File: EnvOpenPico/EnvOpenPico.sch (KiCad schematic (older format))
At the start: 54 parts, among them J2 SKRKAEE020, J3 2.54mm header 01x20, J4 2.54mm header 01x20, J5 Conn_01x03_Male, Q1 Si2329DS, U1 TLV75533PDBVR, U3 RP2040, Y1 3225_4P

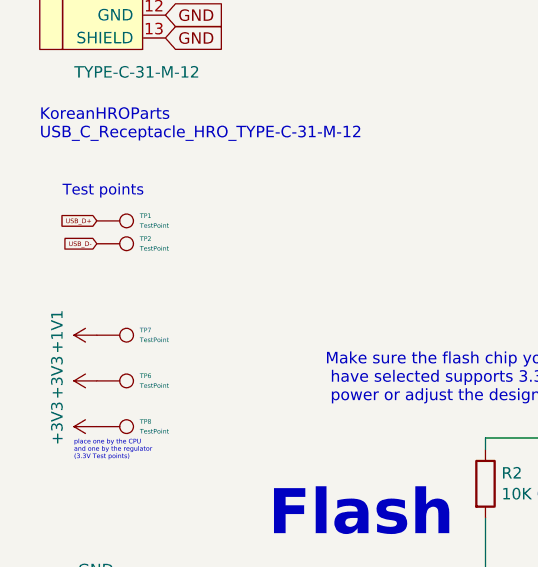
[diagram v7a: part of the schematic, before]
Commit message: Lots of changes, redid elite-c version, added more debug pads to main version and various tweaks among other things.
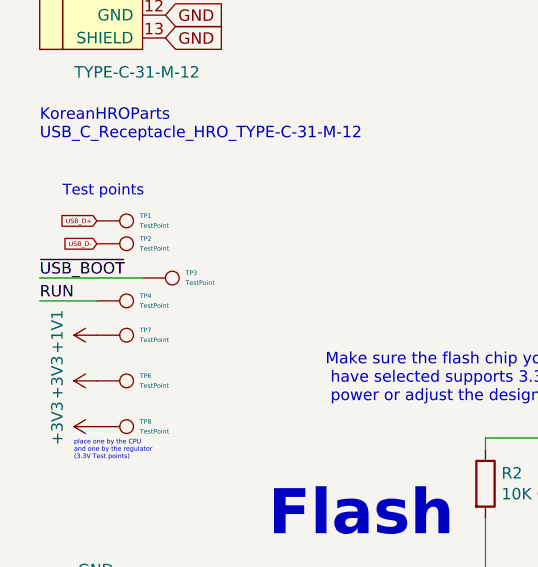
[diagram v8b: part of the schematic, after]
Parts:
- added TP3, TP4: TestPoint, EnvExtras:CustomTestPoint, symbol Connector:TestPoint
- TP1, TP2, TP6, TP7, TP8: footprint TestPoint:TestPoint_Pad_D1.0mm -> EnvExtras:CustomTestPoint
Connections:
- net RUN: now also TP4.1
- net ~USB_BOOT: now also TP3.1
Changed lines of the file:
@@
 F 0 "TP1" V 778 3388 20  0000 L CNN
 F 1 "TestPoint" V 821 3388 20  0000 L CNN
-F 2 "TestPoint:TestPoint_Pad_D1.0mm" H 1000 3200 50  0001 C CNN
+F 2 "EnvExtras:CustomTestPoint" H 1000 3200 50  0001 C CNN
 F 3 "" H 1000 3200 50  0001 C CNN
 F 4 " " H 800 3200 50  0001 C CNN "LCSC"
@@
 F 0 "TP2" V 778 3488 20  0000 L CNN
 F 1 "TestPoint" V 821 3488 20  0000 L CNN
-F 2 "TestPoint:TestPoint_Pad_D1.0mm" H 1000 3300 50  0001 C CNN
+F 2 "EnvExtras:CustomTestPoint" H 1000 3300 50  0001 C CNN
 F 3 "" H 1000 3300 50  0001 C CNN
 F 4 " " H 800 3300 50  0001 C CNN "LCSC"
@@
 F 0 "TP6" V 778 4088 20  0000 L CNN
 F 1 "TestPoint" V 821 4088 20  0000 L CNN
-F 2 "TestPoint:TestPoint_Pad_D1.0mm" H 1000 3900 50  0001 C CNN
+F 2 "EnvExtras:CustomTestPoint" H 1000 3900 50  0001 C CNN
 F 3 "" H 1000 3900 50  0001 C CNN
 F 4 " " H 800 3900 50  0001 C CNN "LCSC"
@@
 F 0 "TP7" V 778 3888 20  0000 L CNN
 F 1 "TestPoint" V 821 3888 20  0000 L CNN
-F 2 "TestPoint:TestPoint_Pad_D1.0mm" H 1000 3700 50  0001 C CNN
+F 2 "EnvExtras:CustomTestPoint" H 1000 3700 50  0001 C CNN
 F 3 "" H 1000 3700 50  0001 C CNN
 F 4 " " H 800 3700 50  0001 C CNN "LCSC"
@@
 F 0 "TP8" V 778 4288 20  0000 L CNN
 F 1 "TestPoint" V 821 4288 20  0000 L CNN
-F 2 "TestPoint:TestPoint_Pad_D1.0mm" H 1000 4100 50  0001 C CNN
+F 2 "EnvExtras:CustomTestPoint" H 1000 4100 50  0001 C CNN
 F 3 "" H 1000 4100 50  0001 C CNN
 F 4 " " H 800 4100 50  0001 C CNN "LCSC"
@@
 Wire Wire Line
 	4350 2150 4350 2550
+$Comp
+L Connector:TestPoint TP3
+U 1 1 61DEBCFE
+P 1000 3450
+F 0 "TP3" V 978 3638 20  0000 L CNN
+F 1 "TestPoint" V 1021 3638 20  0000 L CNN
+F 2 "EnvExtras:CustomTestPoint" H 1200 3450 50  0001 C CNN
+F 3 "" H 1200 3450 50  0001 C CNN
+F 4 " " H 1000 3450 50  0001 C CNN "LCSC"
+	1    1000 3450
+	0    1    1    0
+$EndComp
+$Comp
+L Connector:TestPoint TP4
+U 1 1 61DEBF51
+P 800 3550
+F 0 "TP4" V 778 3738 20  0000 L CNN
+F 1 "TestPoint" V 821 3738 20  0000 L CNN
+F 2 "EnvExtras:CustomTestPoint" H 1000 3550 50  0001 C CNN
+F 3 "" H 1000 3550 50  0001 C CNN
+F 4 " " H 800 3550 50  0001 C CNN "LCSC"
+	1    800  3550
+	0    1    1    0
+$EndComp
+Text Label 550  3450 0    50   ~ 0
+~USB_BOOT
+Wire Wire Line
+	550  3450 1000 3450
+Text Label 550  3550 0    50   ~ 0
+RUN
+Wire Wire Line
+	550  3550 800  3550
 $EndSCHEMATC
